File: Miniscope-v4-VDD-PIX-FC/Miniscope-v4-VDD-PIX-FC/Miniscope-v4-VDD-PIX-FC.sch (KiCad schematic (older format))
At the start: 7 parts, among them J1 Conn_01x01, J2 Conn_01x01, J3 Conn_01x01, U1 MCP1711

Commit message: Finalize v0.1 VDD-PIX FC for fab at OSHPark and PCBWay
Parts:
- gave numbers to parts that had none: 1
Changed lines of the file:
@@
 encoding utf-8
 Sheet 1 1
-Title ""
-Date ""
-Rev ""
-Comp ""
+Title "V4-Miniscope-VDD-Pix-FC"
+Date "2020-09-18"
+Rev "v0.1"
+Comp "Aharoni Lab"
 Comment1 ""
 Comment2 ""
@@
 $EndComp
 $Comp
-L .Inductor:BLM18PG471SN1D L?
+L .Inductor:BLM18PG471SN1D L1
 U 1 1 5F641E2A
 P 5495 2770
-F 0 "L?" V 5680 2770 50  0000 C CNN
+F 0 "L1" V 5680 2770 50  0000 C CNN
 F 1 "BLM18PG471SN1D" H 5545 2620 50  0001 L CNN
 F 2 ".Inductor:L_0603_1608Metric_L" H 5545 3070 50  0001 C CNN

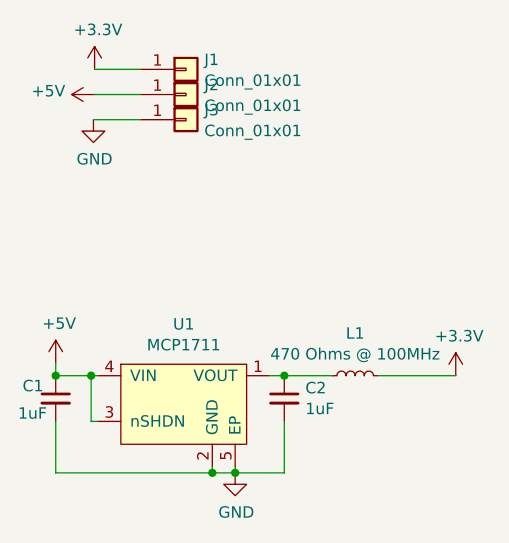
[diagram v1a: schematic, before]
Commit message: Change voltage regulator part number to one with better PSRR
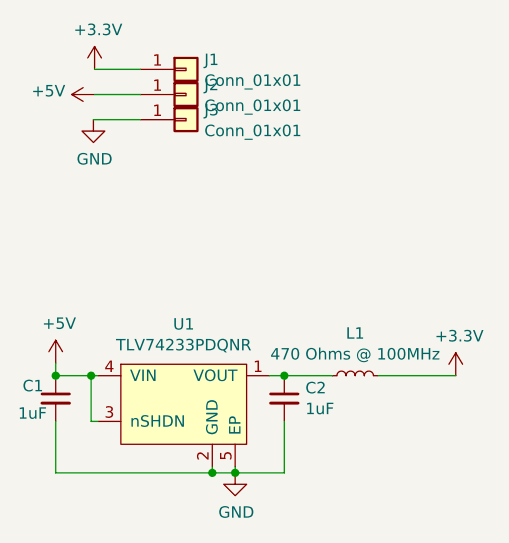
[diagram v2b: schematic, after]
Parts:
- U1: value MCP1711 -> TLV74233PDQNR‎
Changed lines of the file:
@@
 P 4570 2770
 F 0 "U1" H 4745 2995 50  0000 C CNN
-F 1 "MCP1711" H 4745 2904 50  0000 C CNN
+F 1 "TLV74233PDQNR‎" H 4745 2904 50  0000 C CNN
 F 2 ".Package_QFN:UQFN_MCP1711" H 4570 2770 50  0001 C CNN
 F 3 "http://ww1.microchip.com/downloads/en/DeviceDoc/20005415D.pdf" H 4570 2770 50  0001 C CNN

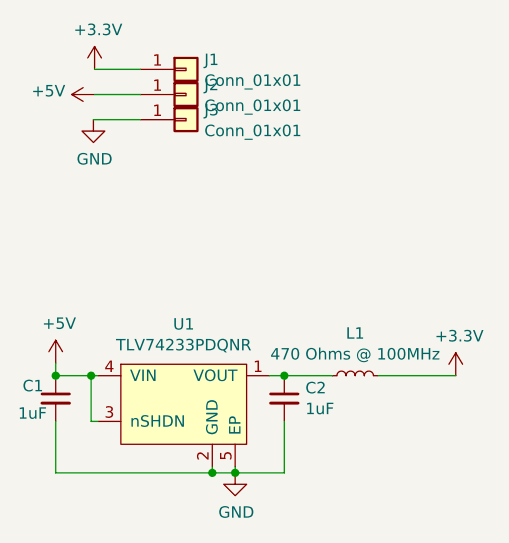
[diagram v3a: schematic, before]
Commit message: Update 3.3V regulator for hotfix PC
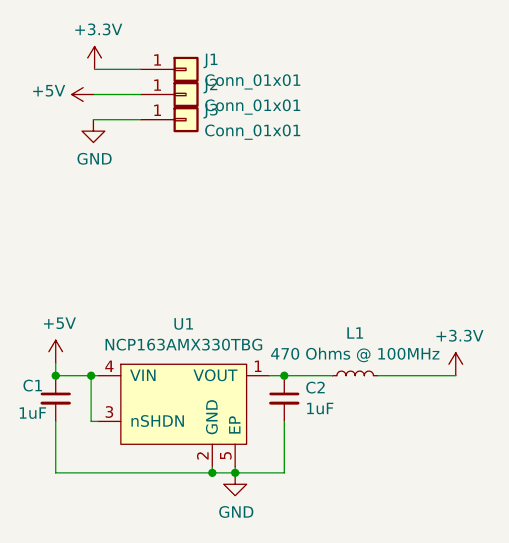
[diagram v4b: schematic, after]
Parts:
- U1: value TLV74233PDQNR‎ -> NCP163AMX330TBG
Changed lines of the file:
@@
 P 4570 2770
 F 0 "U1" H 4745 2995 50  0000 C CNN
-F 1 "TLV74233PDQNR‎" H 4745 2904 50  0000 C CNN
+F 1 "NCP163AMX330TBG" H 4745 2904 50  0000 C CNN
 F 2 ".Package_QFN:UQFN_MCP1711" H 4570 2770 50  0001 C CNN
 F 3 "http://ww1.microchip.com/downloads/en/DeviceDoc/20005415D.pdf" H 4570 2770 50  0001 C CNN
